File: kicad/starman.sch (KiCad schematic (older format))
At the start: 26 parts, among them J1 Barrel_Jack_MountingPin, J2 Conn_02x09_Odd_Even, J3 Conn_02x09_Odd_Even, J4 Conn_02x03_Odd_Even, J5 Conn_01x06, SW1 SW_SPST, SW2 SW_Push, U1 LF50_TO220, U2 LF33_TO220

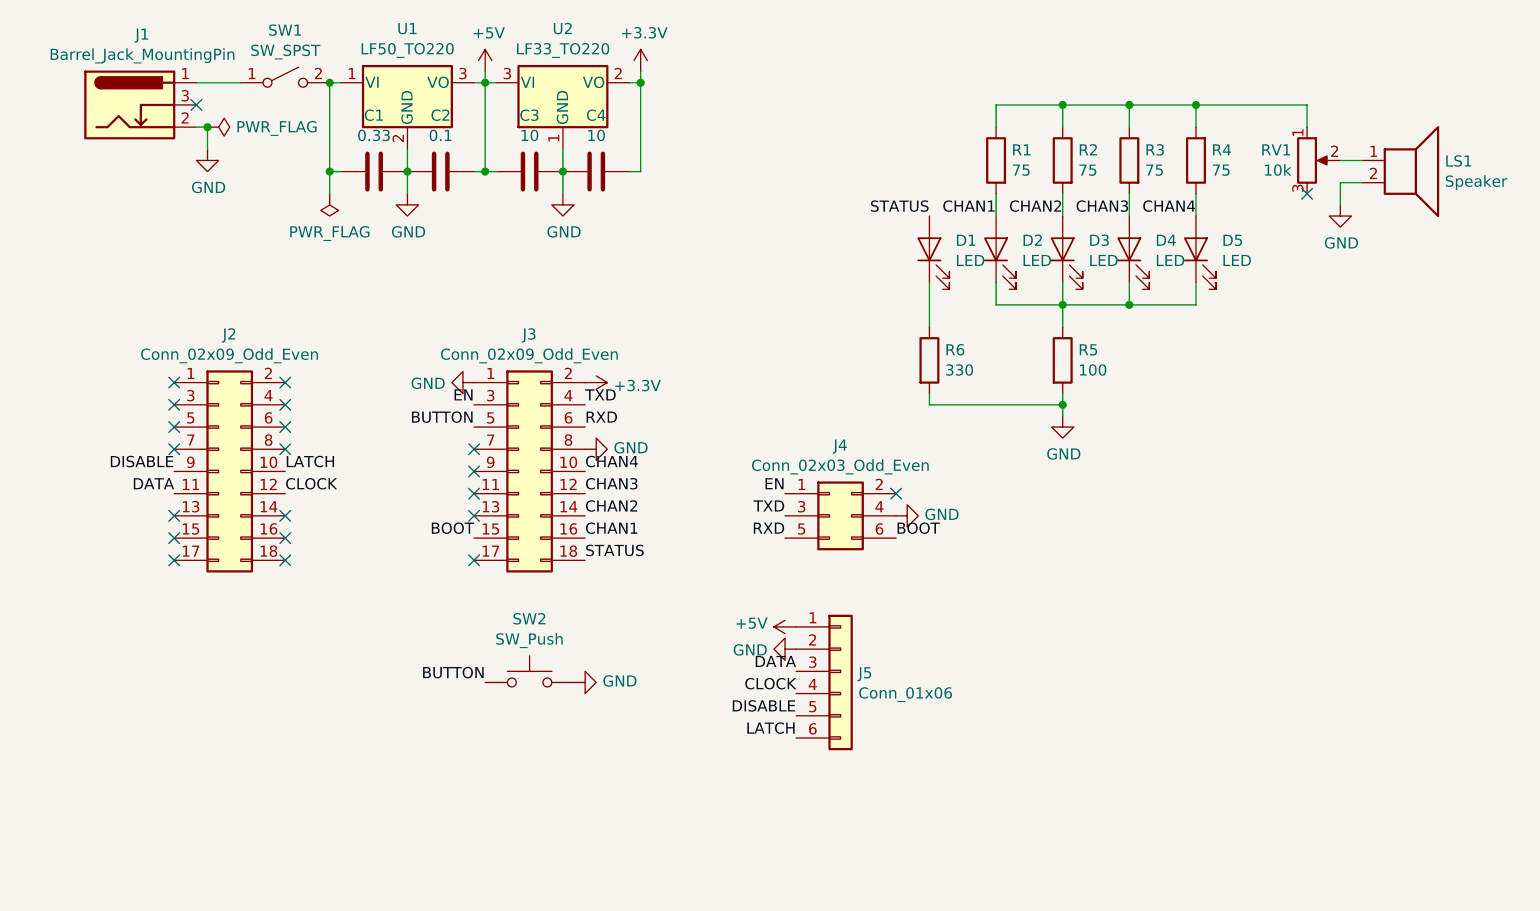
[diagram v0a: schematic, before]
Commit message: Transition to standard ESP32 DevKit mounting
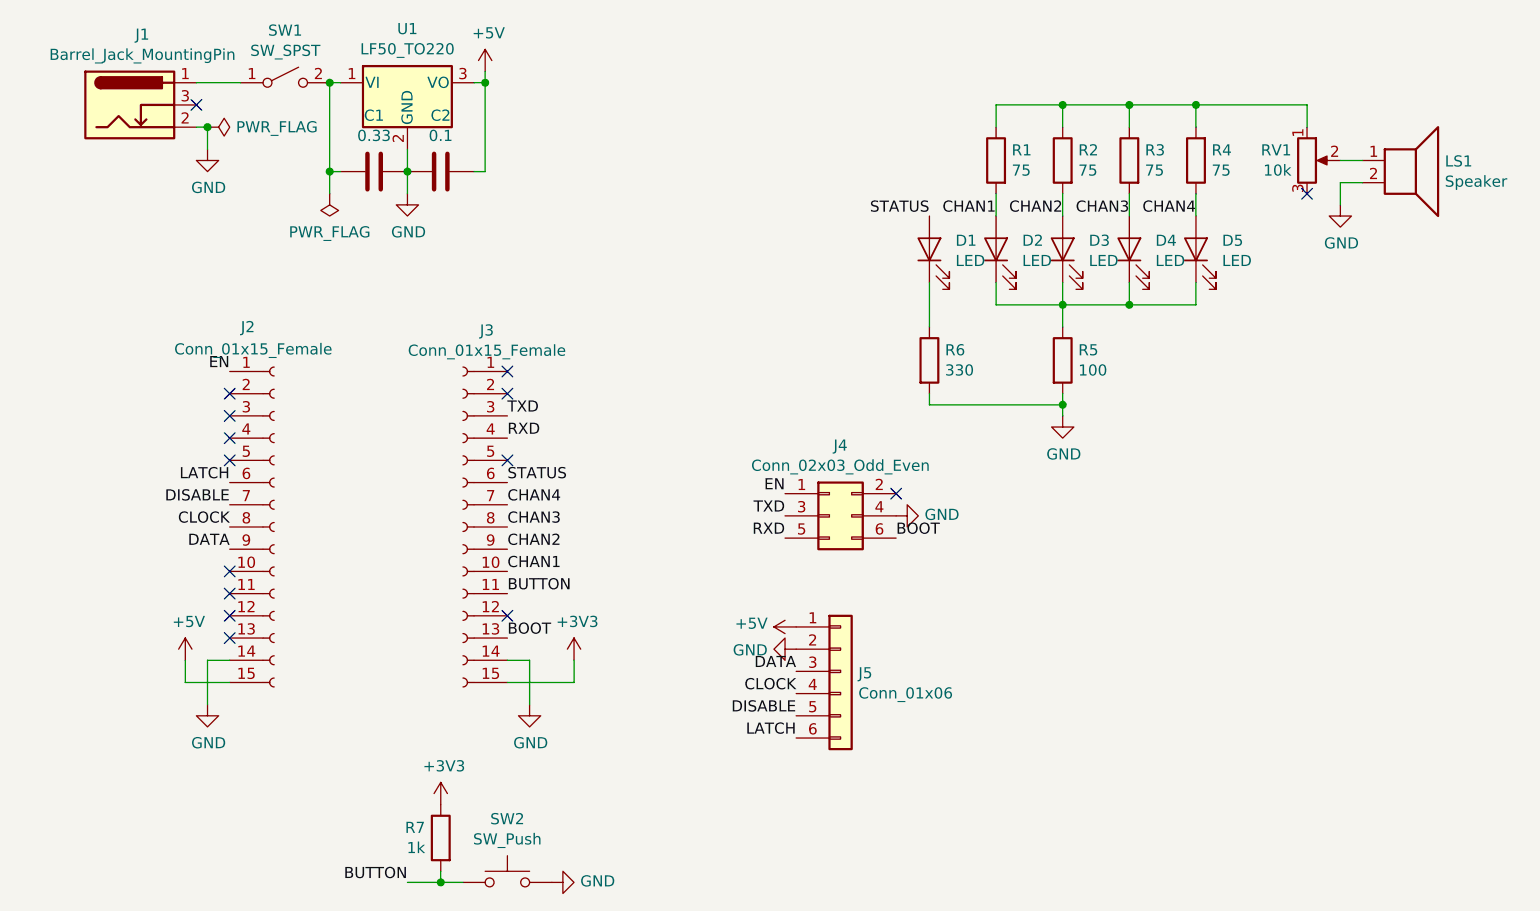
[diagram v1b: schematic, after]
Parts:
- removed C3, C4: 10, Capacitor_THT:C_Disc_D3.0mm_W2.0mm_P2.50mm, symbol Device:C
- removed J2, J3: Conn_02x09_Odd_Even, Connector_PinHeader_2.54mm:PinHeader_2x09_P2.54mm_Vertical, symbol Connector_Generic:Conn_02x09_Odd_Even
- removed U2: LF33_TO220, Package_TO_SOT_THT:TO-220-3_Vertical, symbol Regulator_Linear:AMS1117-3.3
- added J2, J3: Conn_01x15_Female, Connector_PinSocket_2.54mm:PinSocket_1x15_P2.54mm_Vertical, symbol Connector:Conn_01x15_Female
- added R7: 1k, Resistor_THT:R_Axial_DIN0204_L3.6mm_D1.6mm_P7.62mm_Horizontal, symbol Device:R
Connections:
- net +3V3: now also J3.15 (Pin_15), R7.1
- net +5V: now also J2.15 (Pin_15)
- net BOOT: now also J3.13 (Pin_13)
- net BUTTON: now also J3.11 (Pin_11), R7.2
- net CHAN1: now also J3.10 (Pin_10)
- net CHAN2: now also J3.9 (Pin_9)
- net CHAN3: now also J3.8 (Pin_8)
- net CHAN4: now also J3.7 (Pin_7)
- net CLOCK: now also J2.8 (Pin_8)
- net DATA: now also J2.9 (Pin_9)
- net DISABLE: now also J2.7 (Pin_7)
- net EN: now also J2.1 (Pin_1)
- net GND: now also J2.14 (Pin_14), J3.14 (Pin_14)
- net LATCH: now also J2.6 (Pin_6)
- net RXD: now also J3.4 (Pin_4)
- net STATUS: now also J3.6 (Pin_6)
- net TXD: now also J3.3 (Pin_3)
- no-connect marks 22 -> 15
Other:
- moved on the sheet: SW2

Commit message: Minor resistor updates to align with real build
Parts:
- RV1: value 10k -> 1k
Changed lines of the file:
@@
 EELAYER 30 0
 EELAYER END
-$Descr A4 11693 8268
+$Descr USLetter 11000 8500
 encoding utf-8
 Sheet 1 1
@@
 P 7750 1750
 F 0 "RV1" H 7680 1796 50  0000 R CNN
-F 1 "10k" H 7680 1705 50  0000 R CNN
+F 1 "1k" H 7680 1705 50  0000 R CNN
 F 2 "Potentiometer_THT:Potentiometer_Vishay_T73YP_Vertical" H 7750 1750 50  0001 C CNN
 F 3 "~" H 7750 1750 50  0001 C CNN
